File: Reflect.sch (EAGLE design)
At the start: 8 parts

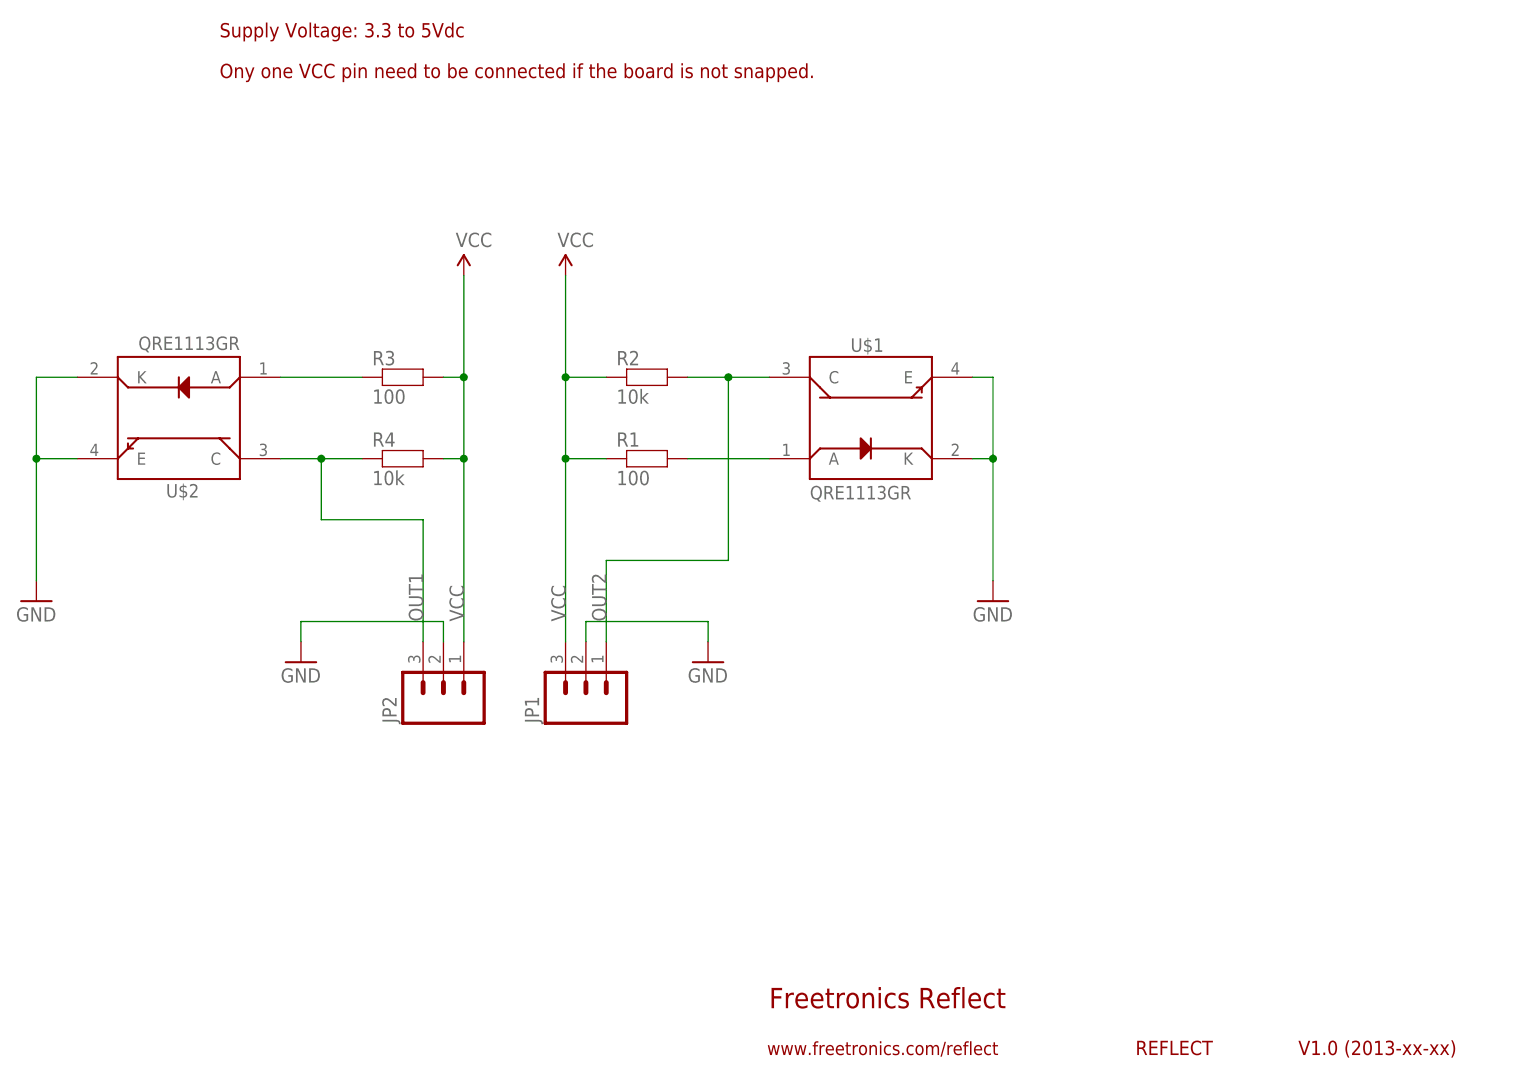
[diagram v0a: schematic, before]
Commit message: Split ground pour into two halves to fix unrouted ground airwire. Added schematic note that although only one VCC pin needs to be connected both ground pins need to be connected if both sensors are used on an unsplit board.
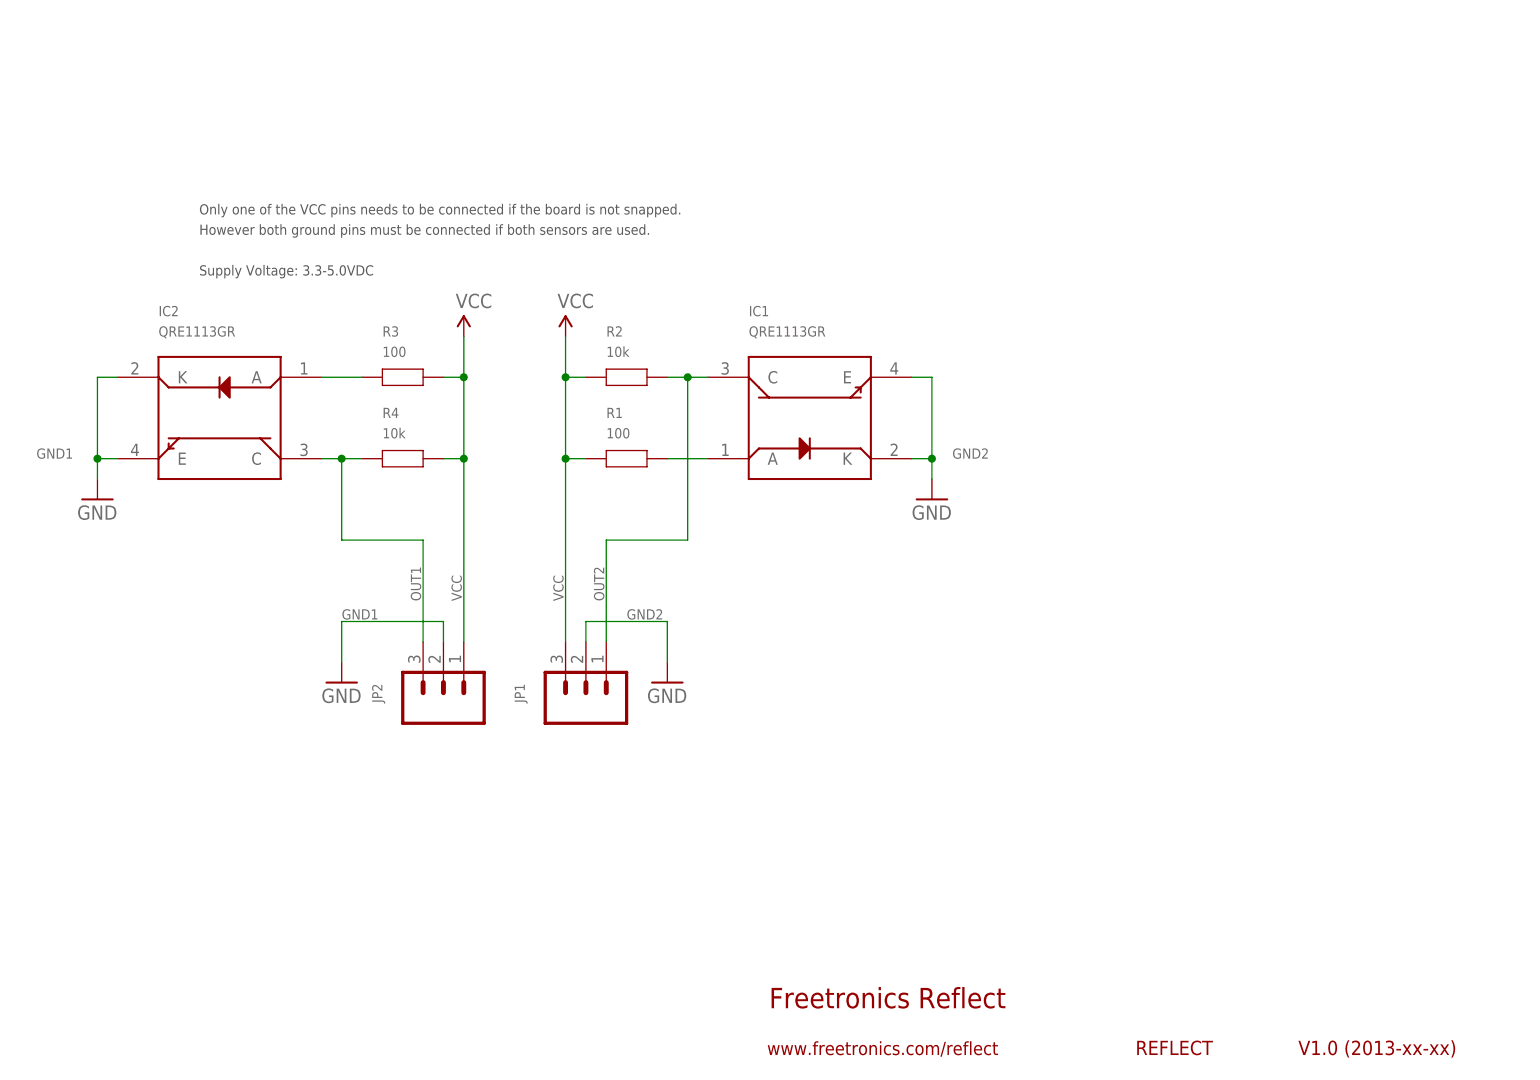
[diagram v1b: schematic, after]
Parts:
- removed U$1, U$2: QRE1113GR, freetronics-original:QRE1113GR
- added IC1, IC2: QRE1113GR, freetronics-original:QRE1113GR
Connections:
- removed net GND: JP1.2, JP2.2, U$1.E, U$1.K, U$2.E, U$2.K
- new net GND1: IC2.E, IC2.K, JP2.2
- new net GND2: IC1.E, IC1.K, JP1.2
- net N$1: now also IC2.A; no longer U$2.A
- net N$3: now also IC1.A; no longer U$1.A
- net OUT1: now also IC2.C; no longer U$2.C
- net OUT2: now also IC1.C; no longer U$1.C
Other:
- note added: "However both ground pins must be connected if both sensors are used."
- note added: "Only one of the VCC pins needs to be connected if the board is not snapped."
- note added: "Supply Voltage: 3.3-5.0VDC"
- note removed: "Ony one VCC pin need to be connected if the board is not snapped."
- note removed: "Supply Voltage: 3.3 to 5Vdc"
- moved on the sheet: R1, R2

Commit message: New version with GNDs connected.
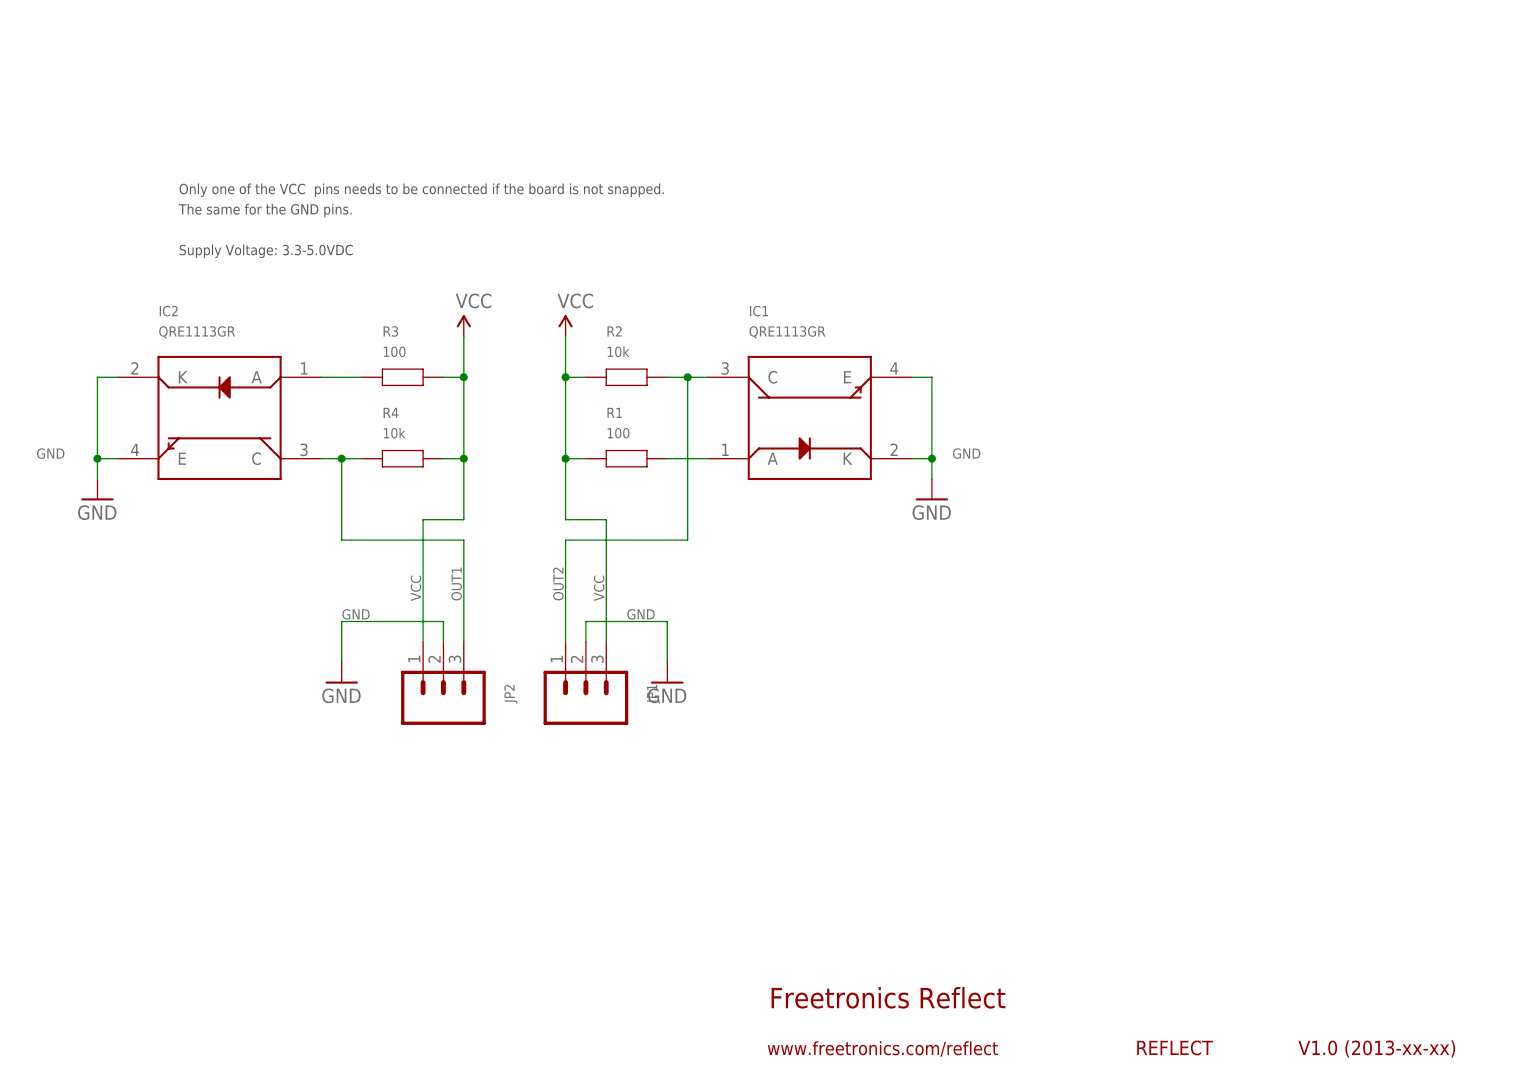
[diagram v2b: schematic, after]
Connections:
- removed net GND1: IC2.E, IC2.K, JP2.2
- removed net GND2: IC1.E, IC1.K, JP1.2
- new net GND: IC1.E, IC1.K, IC2.E, IC2.K, JP1.2, JP2.2
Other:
- note added: "The same for the GND pins."
- note removed: "However both ground pins must be connected if both sensors are used."
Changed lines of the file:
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@@
 <?xml version="1.0" encoding="utf-8"?>
 <!DOCTYPE eagle SYSTEM "eagle.dtd">
-<eagle version="6.4">
+<eagle version="6.5.0">
 <drawing>
 <settings>
@@
 <setting verticaltext="up"/>
 </settings>
-<grid distance="0.1" unitdist="inch" unit="inch" style="lines" multiple="1" display="yes" altdistance="0.01" altunitdist="inch" altunit="inch"/>
+<grid distance="0.1" unitdist="inch" unit="inch" style="lines" multiple="1" display="no" altdistance="0.01" altunitdist="inch" altunit="inch"/>
 <layers>
 <layer number="1" name="Top" color="4" fill="1" visible="no" active="no"/>
@@
 <text x="149.606" y="6.858" size="1.651" layer="94">www.freetronics.com/reflect</text>
 <text x="195.58" y="6.858" size="1.778" layer="94">REFLECT</text>
-<text x="78.74" y="104.14" size="1.27" layer="97">Supply Voltage: 3.3-5.0VDC</text>
+<text x="76.2" y="106.68" size="1.27" layer="97">Supply Voltage: 3.3-5.0VDC</text>
 <frame x1="0" y1="0" x2="248.92" y2="185.42" columns="8" rows="5" layer="94"/>
 <frame x1="147.32" y1="5.08" x2="243.84" y2="17.78" columns="0" rows="0" layer="94" border-left="no" border-top="no" border-right="no" border-bottom="no"/>
 <frame x1="190.5" y1="5.08" x2="213.36" y2="10.16" columns="8" rows="5" layer="94"/>
 <frame x1="213.36" y1="5.08" x2="243.84" y2="10.16" columns="8" rows="5" layer="94"/>
-<text x="78.74" y="111.76" size="1.27" layer="97">Only one of the VCC pins needs to be connected if the board is not snapped.</text>
+<text x="76.2" y="114.3" size="1.27" layer="97">Only one of the VCC  pins needs to be connected if the board is not snapped.</text>
 <wire x1="111.76" y1="91.44" x2="124.46" y2="91.44" width="0.1524" layer="98" style="shortdash"/>
-<text x="78.74" y="109.22" size="1.27" layer="97">However both ground pins must be connected if both sensors are used.</text>
+<text x="76.2" y="111.76" size="1.27" layer="97">The same for the GND pins.</text>
 </plain>
 <instances>
@@
 <instance part="P+1" gate="1" x="124.46" y="96.52"/>
 <instance part="GND2" gate="1" x="170.18" y="76.2"/>
-<instance part="JP1" gate="G$1" x="127" y="50.8" smashed="yes" rot="R90">
-<attribute name="VALUE" x="134.62" y="48.26" size="1.778" layer="96" rot="R90"/>
-<attribute name="NAME" x="119.38" y="50.8" size="1.27" layer="95" rot="R90"/>
+<instance part="JP1" gate="G$1" x="127" y="50.8" smashed="yes" rot="MR90">
+<attribute name="VALUE" x="119.38" y="48.26" size="1.778" layer="96" rot="MR90"/>
+<attribute name="NAME" x="134.62" y="50.8" size="1.27" layer="95" rot="MR90"/>
 </instance>
 <instance part="IC2" gate="G$1" x="81.28" y="86.36" smashed="yes" rot="R180">
@@
 <attribute name="VALUE" x="101.6" y="83.82" size="1.27" layer="96"/>
 </instance>
-<instance part="JP2" gate="G$1" x="109.22" y="50.8" smashed="yes" rot="R90">
-<attribute name="VALUE" x="116.84" y="48.26" size="1.778" layer="96" rot="R90"/>
-<attribute name="NAME" x="101.6" y="50.8" size="1.27" layer="95" rot="R90"/>
+<instance part="JP2" gate="G$1" x="109.22" y="50.8" smashed="yes" rot="MR90">
+<attribute name="VALUE" x="101.6" y="48.26" size="1.778" layer="96" rot="MR90"/>
+<attribute name="NAME" x="116.84" y="50.8" size="1.27" layer="95" rot="MR90"/>
 </instance>
 <instance part="P+2" gate="1" x="111.76" y="96.52"/>
@@
 <segment>
 <pinref part="JP1" gate="G$1" pin="1"/>
-<wire x1="129.54" y1="58.42" x2="129.54" y2="71.12" width="0.1524" layer="91"/>
-<label x="129.286" y="63.5" size="1.27" layer="95" rot="R90"/>
-<wire x1="129.54" y1="71.12" x2="139.7" y2="71.12" width="0.1524" layer="91"/>
+<wire x1="124.46" y1="58.42" x2="124.46" y2="71.12" width="0.1524" layer="91"/>
+<label x="124.206" y="63.5" size="1.27" layer="95" rot="R90"/>
+<wire x1="124.46" y1="71.12" x2="139.7" y2="71.12" width="0.1524" layer="91"/>
 <pinref part="R2" gate="G$1" pin="2"/>
 <pinref part="IC1" gate="G$1" pin="C"/>
@@
 <pinref part="JP1" gate="G$1" pin="3"/>
 <pinref part="P+1" gate="1" pin="VCC"/>
-<wire x1="124.46" y1="58.42" x2="124.46" y2="81.28" width="0.1524" layer="91"/>
-<label x="124.206" y="63.5" size="1.27" layer="95" rot="R90"/>
+<wire x1="129.54" y1="58.42" x2="129.54" y2="73.66" width="0.1524" layer="91"/>
+<wire x1="129.54" y1="73.66" x2="124.46" y2="73.66" width="0.1524" layer="91"/>
+<wire x1="124.46" y1="73.66" x2="124.46" y2="81.28" width="0.1524" layer="91"/>
+<label x="129.286" y="63.5" size="1.27" layer="95" rot="R90"/>
 <pinref part="R1" gate="G$1" pin="1"/>
 <wire x1="124.46" y1="81.28" x2="124.46" y2="91.44" width="0.1524" layer="91"/>
@@
 <wire x1="111.76" y1="96.52" x2="111.76" y2="91.44" width="0.1524" layer="91"/>
 <wire x1="111.76" y1="91.44" x2="111.76" y2="81.28" width="0.1524" layer="91"/>
-<wire x1="111.76" y1="81.28" x2="111.76" y2="58.42" width="0.1524" layer="91"/>
+<wire x1="111.76" y1="81.28" x2="111.76" y2="73.66" width="0.1524" layer="91"/>
+<wire x1="111.76" y1="73.66" x2="106.68" y2="73.66" width="0.1524" layer="91"/>
+<wire x1="106.68" y1="73.66" x2="106.68" y2="58.42" width="0.1524" layer="91"/>
 <pinref part="R4" gate="G$1" pin="2"/>
 <wire x1="109.22" y1="81.28" x2="111.76" y2="81.28" width="0.1524" layer="91"/>
@@
 <junction x="111.76" y="81.28"/>
 <junction x="111.76" y="91.44"/>
-<label x="111.506" y="63.5" size="1.27" layer="95" rot="R90"/>
+<label x="106.426" y="63.5" size="1.27" layer="95" rot="R90"/>
 </segment>
 </net>
@@
 <segment>
 <pinref part="JP2" gate="G$1" pin="3"/>
-<wire x1="106.68" y1="58.42" x2="106.68" y2="71.12" width="0.1524" layer="91"/>
-<label x="106.426" y="63.5" size="1.27" layer="95" rot="R90"/>
+<wire x1="111.76" y1="58.42" x2="111.76" y2="71.12" width="0.1524" layer="91"/>
+<label x="111.506" y="63.5" size="1.27" layer="95" rot="R90"/>
 <pinref part="R4" gate="G$1" pin="1"/>
 <pinref part="IC2" gate="G$1" pin="C"/>
 <wire x1="93.98" y1="81.28" x2="96.52" y2="81.28" width="0.1524" layer="91"/>
 <wire x1="96.52" y1="81.28" x2="99.06" y2="81.28" width="0.1524" layer="91"/>
-<wire x1="106.68" y1="71.12" x2="96.52" y2="71.12" width="0.1524" layer="91"/>
+<wire x1="111.76" y1="71.12" x2="96.52" y2="71.12" width="0.1524" layer="91"/>
 <wire x1="96.52" y1="71.12" x2="96.52" y2="81.28" width="0.1524" layer="91"/>
 <junction x="96.52" y="81.28"/>
@@
 </segment>
 </net>
-<net name="GND1" class="0">
+<net name="GND" class="0">
+<segment>
+<pinref part="JP2" gate="G$1" pin="2"/>
+<wire x1="109.22" y1="58.42" x2="109.22" y2="60.96" width="0.1524" layer="91"/>
+<wire x1="109.22" y1="60.96" x2="96.52" y2="60.96" width="0.1524" layer="91"/>
+<pinref part="GND5" gate="1" pin="GND"/>
+<wire x1="96.52" y1="60.96" x2="96.52" y2="55.88" width="0.1524" layer="91"/>
+<label x="96.52" y="61.214" size="1.27" layer="95"/>
+</segment>
+<segment>
+<pinref part="JP1" gate="G$1" pin="2"/>
+<wire x1="127" y1="58.42" x2="127" y2="60.96" width="0.1524" layer="91"/>
+<pinref part="GND6" gate="1" pin="GND"/>
+<wire x1="127" y1="60.96" x2="137.16" y2="60.96" width="0.1524" layer="91"/>
+<wire x1="137.16" y1="60.96" x2="137.16" y2="55.88" width="0.1524" layer="91"/>
+<label x="132.08" y="61.214" size="1.27" layer="95"/>
+</segment>
+<segment>
+<pinref part="GND2" gate="1" pin="GND"/>
+<wire x1="170.18" y1="78.74" x2="170.18" y2="81.28" width="0.1524" layer="91"/>
+<wire x1="170.18" y1="81.28" x2="170.18" y2="91.44" width="0.1524" layer="91"/>
+<pinref part="IC1" gate="G$1" pin="E"/>
+<wire x1="167.64" y1="91.44" x2="170.18" y2="91.44" width="0.1524" layer="91"/>
+<pinref part="IC1" gate="G$1" pin="K"/>
+<wire x1="167.64" y1="81.28" x2="170.18" y2="81.28" width="0.1524" layer="91"/>
+<junction x="170.18" y="81.28"/>
+<label x="172.72" y="81.28" size="1.27" layer="95"/>
+</segment>
 <segment>
 <pinref part="GND3" gate="1" pin="GND"/>
@@
 <label x="58.42" y="81.28" size="1.27" layer="95"/>
 </segment>
-<segment>
-<pinref part="JP2" gate="G$1" pin="2"/>
-<wire x1="109.22" y1="58.42" x2="109.22" y2="60.96" width="0.1524" layer="91"/>
-<wire x1="109.22" y1="60.96" x2="96.52" y2="60.96" width="0.1524" layer="91"/>
-<pinref part="GND5" gate="1" pin="GND"/>
-<wire x1="96.52" y1="60.96" x2="96.52" y2="55.88" width="0.1524" layer="91"/>
-<label x="96.52" y="61.214" size="1.27" layer="95"/>
-</segment>
-</net>
-<net name="GND2" class="0">
-<segment>
-<pinref part="JP1" gate="G$1" pin="2"/>
-<wire x1="127" y1="58.42" x2="127" y2="60.96" width="0.1524" layer="91"/>
-<pinref part="GND6" gate="1" pin="GND"/>
-<wire x1="127" y1="60.96" x2="137.16" y2="60.96" width="0.1524" layer="91"/>
-<wire x1="137.16" y1="60.96" x2="137.16" y2="55.88" width="0.1524" layer="91"/>
-<label x="132.08" y="61.214" size="1.27" layer="95"/>
-</segment>
-<segment>
-<pinref part="GND2" gate="1" pin="GND"/>
-<wire x1="170.18" y1="78.74" x2="170.18" y2="81.28" width="0.1524" layer="91"/>
-<wire x1="170.18" y1="81.28" x2="170.18" y2="91.44" width="0.1524" layer="91"/>
-<pinref part="IC1" gate="G$1" pin="E"/>
-<wire x1="167.64" y1="91.44" x2="170.18" y2="91.44" width="0.1524" layer="91"/>
-<pinref part="IC1" gate="G$1" pin="K"/>
-<wire x1="167.64" y1="81.28" x2="170.18" y2="81.28" width="0.1524" layer="91"/>
-<junction x="170.18" y="81.28"/>
-<label x="172.72" y="81.28" size="1.27" layer="95"/>
-</segment>
-</net>
+</net>
